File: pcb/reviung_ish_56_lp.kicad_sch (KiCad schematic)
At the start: 126 parts, among them J1 BATTERY1, J2 BATTERY2, SW1 POWER, SW2 RESET, U1 ProMicro

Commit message: Switch to standard mounting hole footprints; bump version to 0.95
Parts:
- H1, H2, H3, H4, H5, H6, H7, H8: symbol horizon-components:Hole_Pad -> Mechanical:MountingHole
- J1: value BATTERY1 -> BAT
- J2: value BATTERY2 -> BATTERY
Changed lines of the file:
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@@
     (pin "2")
   )
-  (symbol (lib_id "horizon-components:Hole_Pad") (at 259.715 154.305 0) (unit 1)
+  (symbol (lib_id "Mechanical:MountingHole") (at 259.715 154.305 0) (unit 1)
     (in_bom yes) (on_board yes) (fields_autoplaced)
     (property "Reference" "H8" (id 0) (at 262.255 151.7649 0)
@@
       (effects (font (size 1.27 1.27)) hide)
     )
-    (property "Datasheet" "" (id 3) (at 259.715 154.305 0)
-      (effects (font (size 1.27 1.27)) hide)
-    )
-    (pin "1")
+    (property "Datasheet" "~" (id 3) (at 259.715 154.305 0)
+      (effects (font (size 1.27 1.27)) hide)
+    )
   )
   (symbol (lib_id "Device:D") (at 314.96 28.575 90) (unit 1)
@@
     (pin "2")
   )
-  (symbol (lib_id "horizon-components:Hole_Pad") (at 226.695 142.875 0) (unit 1)
+  (symbol (lib_id "Mechanical:MountingHole") (at 226.695 142.875 0) (unit 1)
     (in_bom yes) (on_board yes) (fields_autoplaced)
     (property "Reference" "H2" (id 0) (at 229.235 140.3349 0)
@@
       (effects (font (size 1.27 1.27)) hide)
     )
-    (property "Datasheet" "" (id 3) (at 226.695 142.875 0)
-      (effects (font (size 1.27 1.27)) hide)
-    )
-    (pin "1")
+    (property "Datasheet" "~" (id 3) (at 226.695 142.875 0)
+      (effects (font (size 1.27 1.27)) hide)
+    )
   )
   (symbol (lib_id "Switch:SW_Push") (at 25.4 24.765 0) (unit 1)
@@
     (in_bom yes) (on_board yes)
     (property "Reference" "J2" (id 0) (at 119.38 168.91 0))
-    (property "Value" "BATTERY2" (id 1) (at 119.38 171.45 0))
+    (property "Value" "BATTERY" (id 1) (at 119.38 171.45 0))
     (property "Footprint" "Connector_JST:JST_PH_S2B-PH-K_1x02_P2.00mm_Horizontal" (id 2) (at 119.38 177.165 0)
       (effects (font (size 1.27 1.27)) hide)
@@
     (pin "2")
   )
-  (symbol (lib_id "horizon-components:Hole_Pad") (at 227.33 154.305 0) (unit 1)
+  (symbol (lib_id "Mechanical:MountingHole") (at 227.33 154.305 0) (unit 1)
     (in_bom yes) (on_board yes) (fields_autoplaced)
     (property "Reference" "H6" (id 0) (at 229.87 151.7649 0)
@@
       (effects (font (size 1.27 1.27)) hide)
     )
-    (property "Datasheet" "" (id 3) (at 227.33 154.305 0)
-      (effects (font (size 1.27 1.27)) hide)
-    )
-    (pin "1")
+    (property "Datasheet" "~" (id 3) (at 227.33 154.305 0)
+      (effects (font (size 1.27 1.27)) hide)
+    )
   )
   (symbol (lib_id "Device:D") (at 196.85 28.575 90) (unit 1)
@@
     (pin "3")
   )
-  (symbol (lib_id "horizon-components:Hole_Pad") (at 259.715 144.145 0) (unit 1)
+  (symbol (lib_id "Mechanical:MountingHole") (at 259.715 144.145 0) (unit 1)
     (in_bom yes) (on_board yes)
     (property "Reference" "H4" (id 0) (at 262.255 141.6049 0)
@@
       (effects (font (size 1.27 1.27)) hide)
     )
-    (property "Datasheet" "" (id 3) (at 259.715 144.145 0)
-      (effects (font (size 1.27 1.27)) hide)
-    )
-    (pin "1")
-  )
-  (symbol (lib_id "horizon-components:Hole_Pad") (at 243.205 144.145 0) (unit 1)
+    (property "Datasheet" "~" (id 3) (at 259.715 144.145 0)
+      (effects (font (size 1.27 1.27)) hide)
+    )
+  )
+  (symbol (lib_id "Mechanical:MountingHole") (at 243.205 144.145 0) (unit 1)
     (in_bom yes) (on_board yes) (fields_autoplaced)
     (property "Reference" "H3" (id 0) (at 245.745 141.6049 0)
@@
       (effects (font (size 1.27 1.27)) hide)
     )
-    (property "Datasheet" "" (id 3) (at 243.205 144.145 0)
-      (effects (font (size 1.27 1.27)) hide)
-    )
-    (pin "1")
+    (property "Datasheet" "~" (id 3) (at 243.205 144.145 0)
+      (effects (font (size 1.27 1.27)) hide)
+    )
   )
   (symbol (lib_id "Device:D") (at 175.26 64.135 90) (unit 1)
@@
     (pin "2")
   )
-  (symbol (lib_id "horizon-components:Hole_Pad") (at 210.185 142.875 0) (unit 1)
+  (symbol (lib_id "Mechanical:MountingHole") (at 210.185 142.875 0) (unit 1)
     (in_bom yes) (on_board yes) (fields_autoplaced)
     (property "Reference" "H1" (id 0) (at 212.725 140.3349 0)
@@
       (effects (font (size 1.27 1.27)) hide)
     )
-    (property "Datasheet" "" (id 3) (at 210.185 142.875 0)
-      (effects (font (size 1.27 1.27)) hide)
-    )
-    (pin "1")
+    (property "Datasheet" "~" (id 3) (at 210.185 142.875 0)
+      (effects (font (size 1.27 1.27)) hide)
+    )
   )
   (symbol (lib_id "Switch:SW_Push") (at 237.49 108.585 0) (unit 1)
@@
     (pin "2")
   )
-  (symbol (lib_id "horizon-components:Hole_Pad") (at 243.205 154.305 0) (unit 1)
+  (symbol (lib_id "Mechanical:MountingHole") (at 243.205 154.305 0) (unit 1)
     (in_bom yes) (on_board yes) (fields_autoplaced)
     (property "Reference" "H7" (id 0) (at 245.745 151.7649 0)
@@
       (effects (font (size 1.27 1.27)) hide)
     )
-    (property "Datasheet" "" (id 3) (at 243.205 154.305 0)
-      (effects (font (size 1.27 1.27)) hide)
-    )
-    (pin "1")
-  )
-  (symbol (lib_id "horizon-components:Hole_Pad") (at 210.82 154.305 0) (unit 1)
+    (property "Datasheet" "~" (id 3) (at 243.205 154.305 0)
+      (effects (font (size 1.27 1.27)) hide)
+    )
+  )
+  (symbol (lib_id "Mechanical:MountingHole") (at 210.82 154.305 0) (unit 1)
     (in_bom yes) (on_board yes) (fields_autoplaced)
     (property "Reference" "H5" (id 0) (at 213.36 151.7649 0)
@@
       (effects (font (size 1.27 1.27)) hide)
     )
-    (property "Datasheet" "" (id 3) (at 210.82 154.305 0)
-      (effects (font (size 1.27 1.27)) hide)
-    )
-    (pin "1")
+    (property "Datasheet" "~" (id 3) (at 210.82 154.305 0)
+      (effects (font (size 1.27 1.27)) hide)
+    )
   )
   (symbol (lib_id "Switch:SW_Push") (at 309.88 24.765 0) (unit 1)
@@
     (in_bom yes) (on_board yes)
     (property "Reference" "J1" (id 0) (at 119.38 156.845 0))
-    (property "Value" "BATTERY1" (id 1) (at 119.38 159.385 0))
+    (property "Value" "BAT" (id 1) (at 119.38 159.385 0))
     (property "Footprint" "Connector_PinHeader_2.54mm:PinHeader_1x02_P2.54mm_Vertical" (id 2) (at 119.38 165.1 0)
       (effects (font (size 1.27 1.27)) hide)
@@
     )
     (path "/cf7982c8-fe2f-4bb4-b68d-47b7f2e5ae7c"
-      (reference "J1") (unit 1) (value "BATTERY1") (footprint "Connector_PinHeader_2.54mm:PinHeader_1x02_P2.54mm_Vertical")
+      (reference "J1") (unit 1) (value "BAT") (footprint "Connector_PinHeader_2.54mm:PinHeader_1x02_P2.54mm_Vertical")
     )
     (path "/63908310-7b5c-458b-8e2f-7a1e1f55002f"
-      (reference "J2") (unit 1) (value "BATTERY2") (footprint "Connector_JST:JST_PH_S2B-PH-K_1x02_P2.00mm_Horizontal")
+      (reference "J2") (unit 1) (value "BATTERY") (footprint "Connector_JST:JST_PH_S2B-PH-K_1x02_P2.00mm_Horizontal")
     )
     (path "/391548d8-cdad-4c5e-8136-7493f8147303"

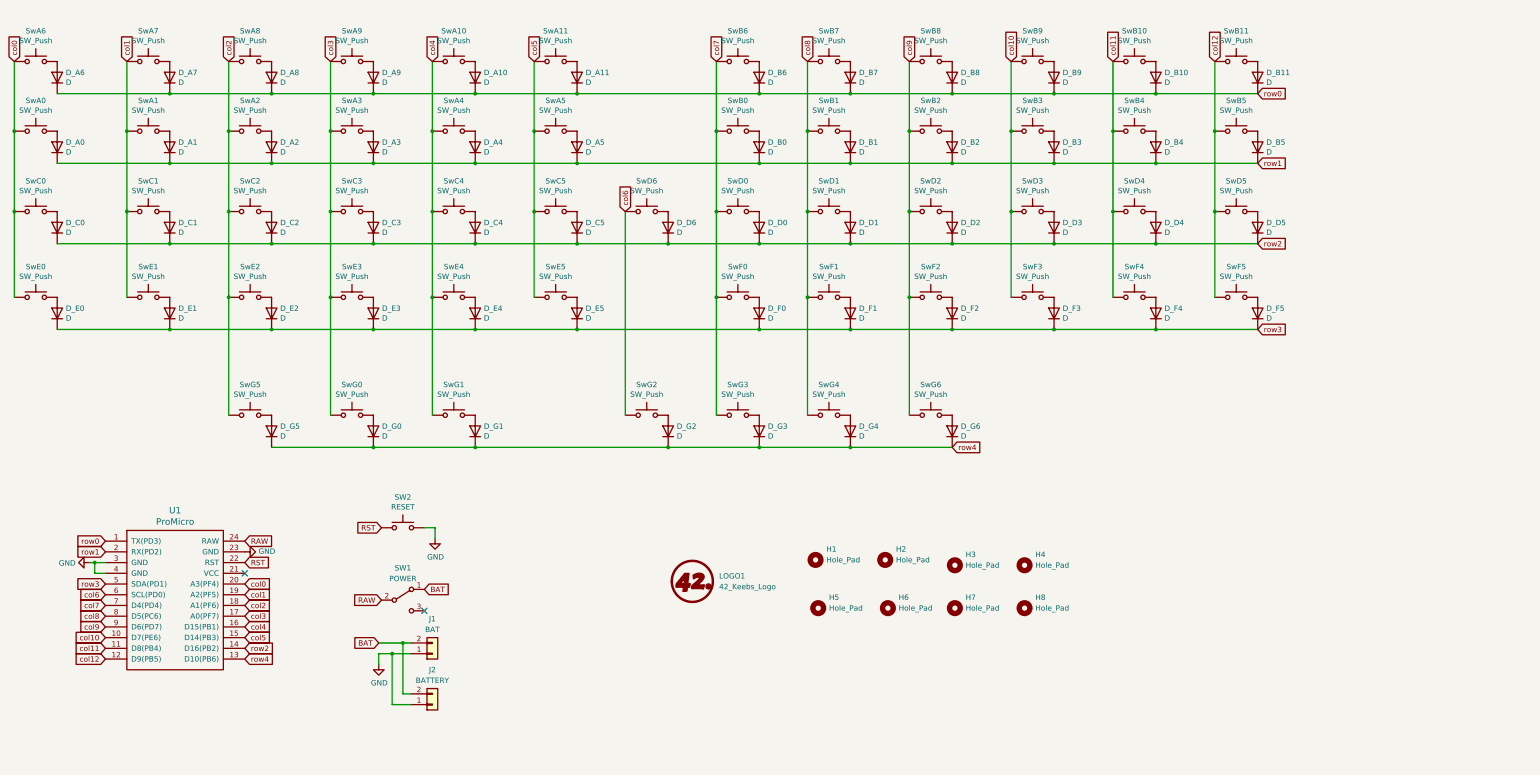
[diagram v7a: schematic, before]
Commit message: Use 1.5u space; improve outline; add power switch and battery connectors; improve routing
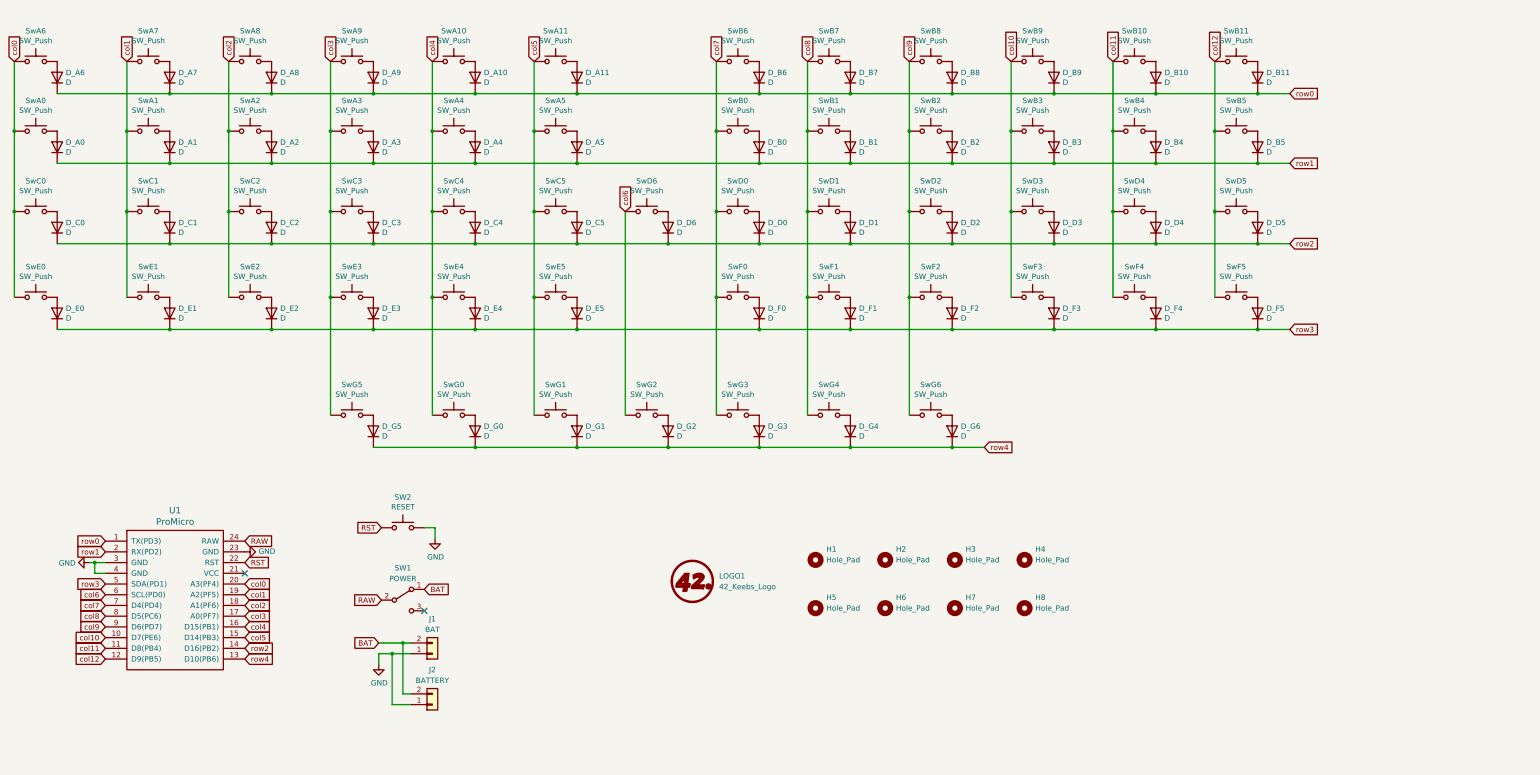
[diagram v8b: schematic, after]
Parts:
- H1, H2, H3, H4, H5, H6, H7, H8: footprint MountingHole:MountingHole_2.2mm_M2_Pad_Via -> MountingHole:MountingHole_2.2mm_M2_ISO7380_Pad
- SwA0, SwA1, SwA10, SwA11, SwA2, SwA3, SwA4, SwA5, SwA6, SwA7, SwA8, SwA9, SwB0, SwB1, SwB10, SwB11, SwB2, SwB3, SwB4, SwB5, SwB6, SwB7, SwB8, SwB9, SwC0, SwC1, SwC2, SwC3, SwC5, SwD0, SwD2, SwD3, SwD4, SwD5, SwD6, SwE0, SwE1, SwE2, SwE3, SwE4, SwE5, SwF0, SwF1, SwF2, SwF3, SwF4, SwF5, SwG0, SwG1, SwG3, SwG4, SwG5, SwG6: footprint 42keebs:Kailh_socket_PG1350 -> 42keebs:Kailh_socket_PG1350_1u_sw_cap
- SwC4, SwD1: footprint 42keebs:Kailh_socket_PG1350 -> 42keebs:Kailh_socket_PG1350_1u_sw_cap_home
- SwG2: footprint keeblib:Kailh-PG1350-2uStabilizer_socket -> 42keebs:Kailh_socket_PG1350_1.5u_sw_cap
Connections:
- net col2: no longer SwG5.1
- net col3: now also SwG5.1; no longer SwG0.1
- net col4: now also SwG0.1; no longer SwG1.1
- net col5: now also SwG1.1
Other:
- moved on the sheet: D_G0, D_G1, D_G5, H3, H4, H5, H6, SwG0, SwG1, SwG5
